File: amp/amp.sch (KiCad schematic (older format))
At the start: 48 parts, among them J1 Conn_01x05, J2 DUAL_RCA, SW1 SW_SPST_GND, T1 Transformer_1P_1S, T2 Transformer_1P_1S, T3 Transformer_PT190.2, U1 6CY7, U2 6CY7, U3 6CA4

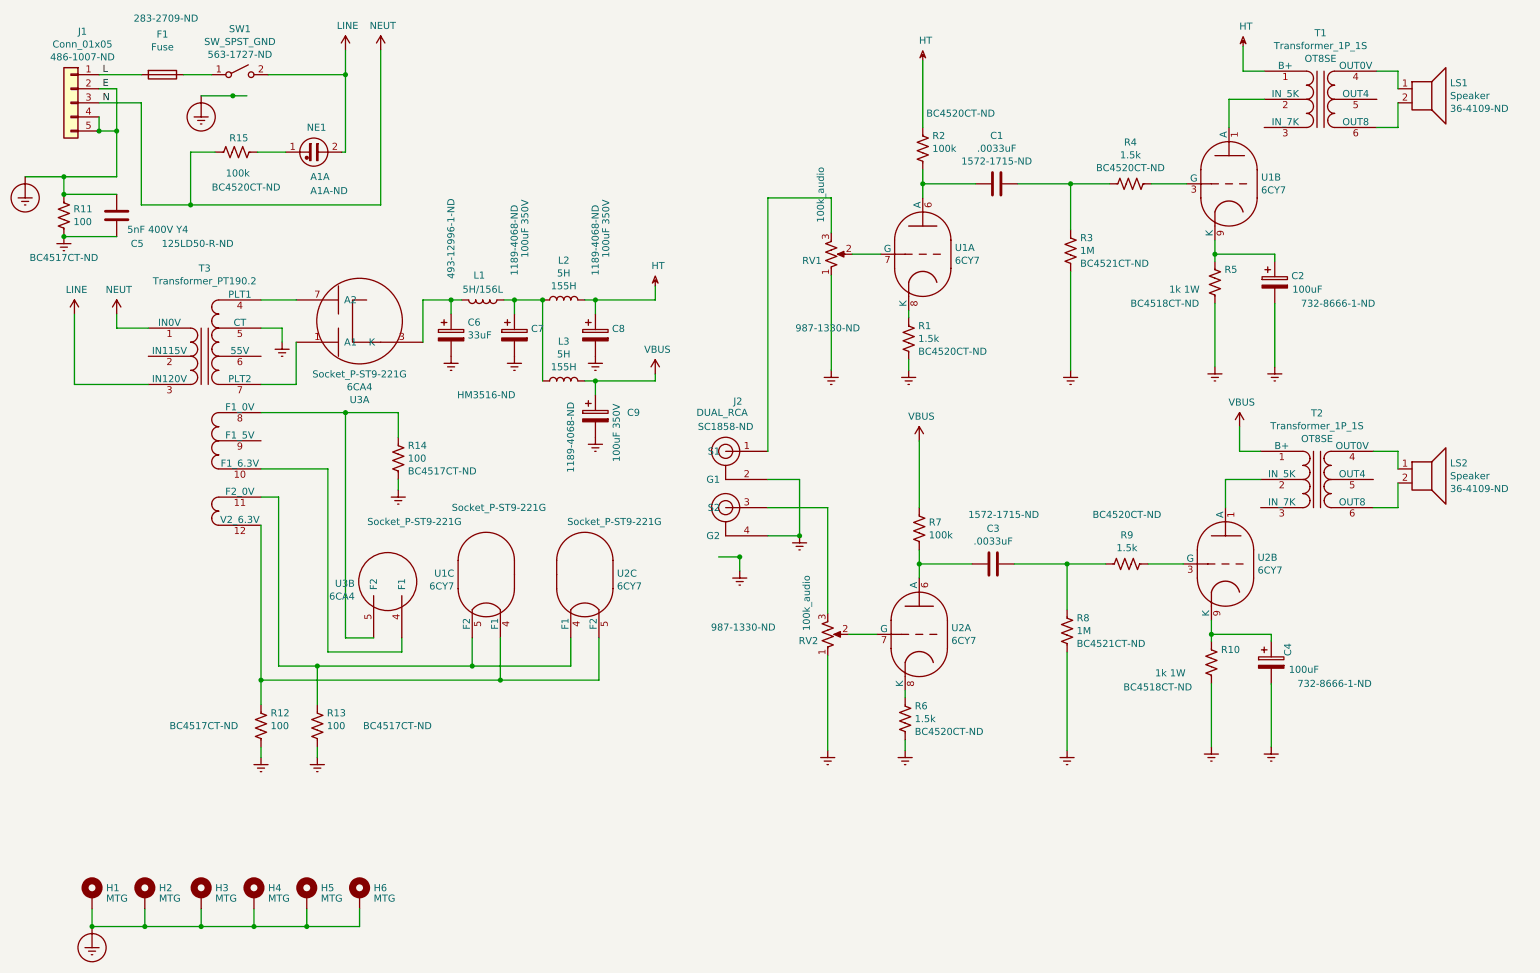
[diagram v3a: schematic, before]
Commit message: Fix 1.5K part number, add PDF schematic
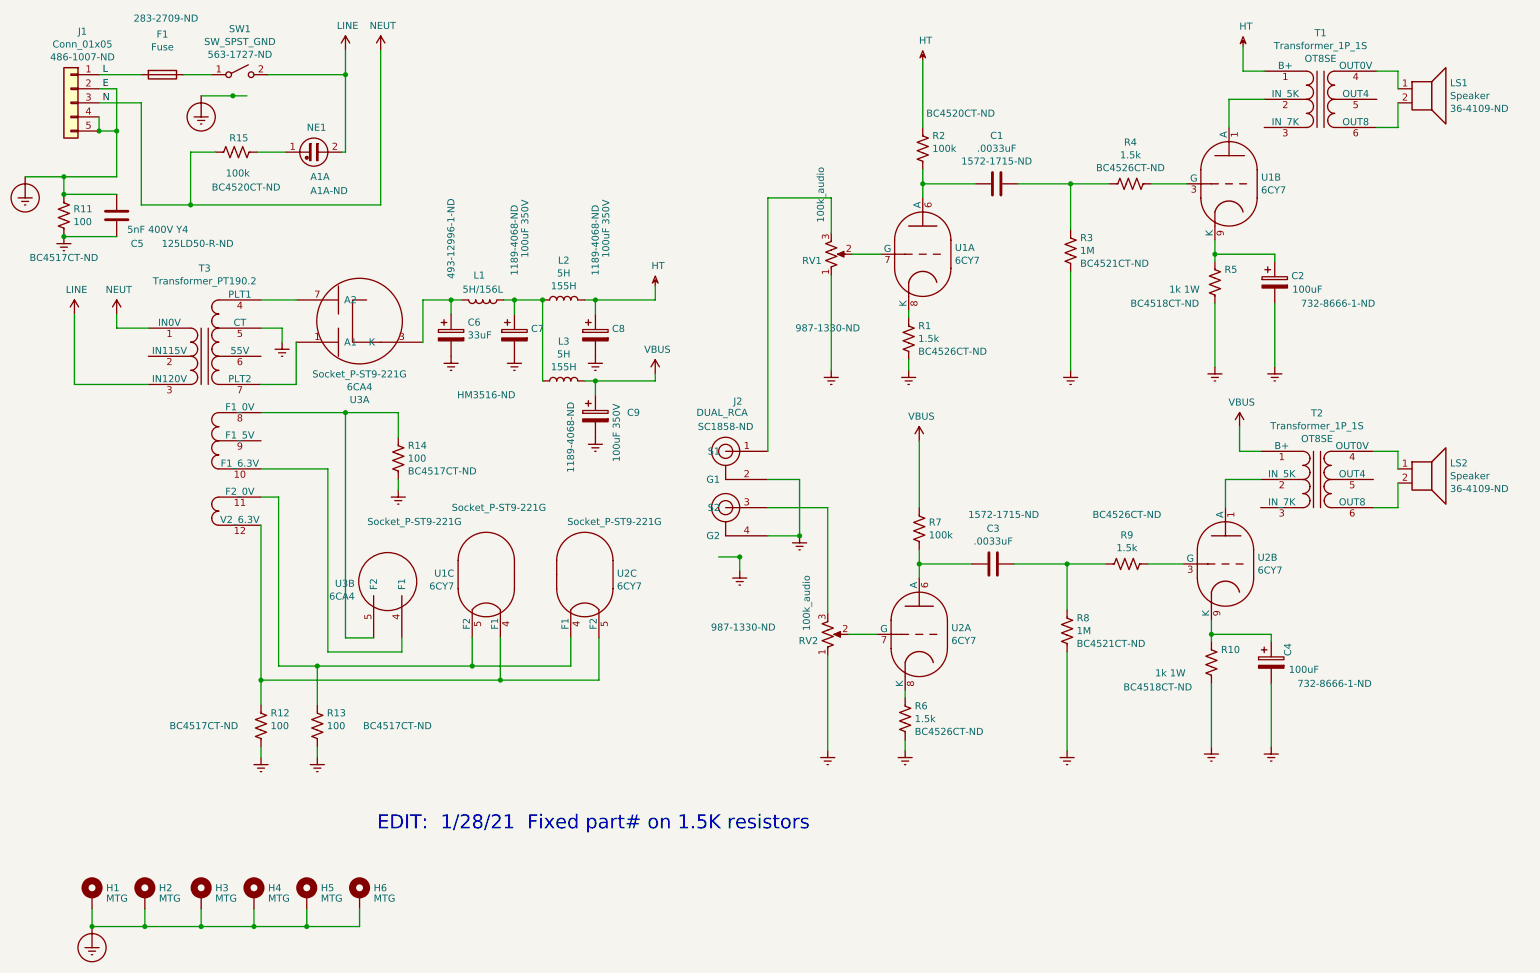
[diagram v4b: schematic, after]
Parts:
- R1, R4, R6, R9: CatNo BC4520CT-ND -> BC4526CT-ND
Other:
- note added: "EDIT: 1/28/21 Fixed part# on 1.5K resistors"
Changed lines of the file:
@@
 F 2 "Resistor_THT:R_Axial_DIN0414_L11.9mm_D4.5mm_P15.24mm_Horizontal" V 7015 3115 50  0001 C CNN
 F 3 "~" H 6975 3125 50  0001 C CNN
-F 4 "BC4520CT-ND" H 7043 3034 50  0000 L CNN "CatNo"
+F 4 "BC4526CT-ND" H 7043 3034 50  0000 L CNN "CatNo"
 F 5 "DigiKey" H 6975 3125 50  0001 C CNN "Vendor"
 	1    6975 3125
@@
 F 2 "Resistor_THT:R_Axial_DIN0414_L11.9mm_D4.5mm_P15.24mm_Horizontal" V 8590 2015 50  0001 C CNN
 F 3 "~" H 8550 2025 50  0001 C CNN
-F 4 "BC4520CT-ND" V 8437 2025 50  0000 C CNN "CatNo"
+F 4 "BC4526CT-ND" V 8437 2025 50  0000 C CNN "CatNo"
 F 5 "DigiKey" V 8550 2025 50  0001 C CNN "Vendor"
 	1    8550 2025
@@
 F 2 "Resistor_THT:R_Axial_DIN0414_L11.9mm_D4.5mm_P15.24mm_Horizontal" V 6990 5815 50  0001 C CNN
 F 3 "~" H 6950 5825 50  0001 C CNN
-F 4 "BC4520CT-ND" H 7018 5734 50  0000 L CNN "CatNo"
+F 4 "BC4526CT-ND" H 7018 5734 50  0000 L CNN "CatNo"
 F 5 "DigiKey" H 6950 5825 50  0001 C CNN "Vendor"
 	1    6950 5825
@@
 F 2 "Resistor_THT:R_Axial_DIN0414_L11.9mm_D4.5mm_P15.24mm_Horizontal" V 8565 4715 50  0001 C CNN
 F 3 "~" H 8525 4725 50  0001 C CNN
-F 4 "BC4520CT-ND" V 8175 4725 50  0000 C CNN "CatNo"
+F 4 "BC4526CT-ND" V 8175 4725 50  0000 C CNN "CatNo"
 	1    8525 4725
 	0    1    1    0
@@
 Wire Wire Line
 	1950 1400 2175 1400
+Text Notes 3200 6625 0    100  ~ 0
+EDIT:  1/28/21  Fixed part# on 1.5K resistors
 $EndSCHEMATC
